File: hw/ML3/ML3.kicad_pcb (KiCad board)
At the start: 2 copper layers, 130 x 56 mm, 73 parts, among them J1 DE9_Receptacle, J2 PJ-102AH, J3 Conn_01x20, J4 Conn_01x02, Q1 DMG2305UX-13, SW0 TS04-66-55-BK-160-SMT, T1 Transformer_1P_1S, T2 Transformer_1P_1S, U1 LMV324 (Actually LTV9161), U2 LTV-356T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

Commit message: Added documentation about isolation - no board changes
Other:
- board text added: "NOTE: This break creates electrical isolation between the radio and the rest of the board."
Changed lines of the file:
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@@
+	)
+	(gr_line
+		(start 218.5 33.25)
+		(end 219.5 43.5)
+		(stroke
+			(width 0.15)
+			(type default)
+		)
+		(layer "Dwgs.User")
 	)
 	(gr_line
@@
 	)
 	(gr_line
-		(start 232.45 38.25)
-		(end 243.5 57.25)
+		(start 260 41)
+		(end 250 66.75)
 		(stroke
 			(width 0.3)
@@
 	)
 	(gr_text "J1: Radio connection (DB9)"
-		(at 223 37.25 0)
+		(at 257 38.25 0)
 		(layer "Dwgs.User")
 		(effects
@@
 		)
 	)
+	(gr_text "NOTE: This break creates electrical \nisolation between the radio and the \nrest of the board."
+		(at 205.5 33 0)
+		(layer "Dwgs.User")
+		(effects
+			(font
+				(size 1.5 1.5)
+				(thickness 0.2)
+				(bold yes)
+			)
+			(justify left bottom)
+		)
+	)
 	(gr_text "Micro USB Connection\n(NOTE: Bonded to Pico Pi daughter\ncard, so elevated from main PCB\nby 1.0mm)"
 		(at 137 37 0)
@@
 		)
 	)
-	(gr_text_box "External Connectors:\n1. J1 is a DB9 audio/signal connector connector.\n2. J2 is a 5.5mm DC power connector for +12V.  Center positive.\n3. The micro USB connector on the Pi Pico daughter card must be accessible through case.\n\nIndicator Notes:\n4. There are three SMD LEDs (D1, D3, D4).  External visibilty is required.\n\nThermal Notes:\n5. Air flow in the area of the LDO regulator (U3) is necessary.\n\nOther notes:\n6. Connector J3 is for testing.  Pin header will be populated.\n7. Trim protentiometers RV1, RV2 do not need to be accessible through case.\n8. Switch SW0 is used for programming and does not need to accessible through case.\n9. Connector J4 is an additional power output that is only used for diagnostics - not accessible through case.\n10. There are through-hole components on the PCB that result in leads/solder protroding from the bottom of the PCB. Leave about 5mm of clearance under the board.\n11. User adjustments on the top side of the PCB will be necessary during initial instalation (switches, trim pots).  The top of the case must be fairly easy to remove. "
+	(gr_text_box "External Connectors:\n1. J1 is a DB9 audio/signal connector connector.\n2. J2 is a 5.5mm DC power connector for +12V.  Center positive.\n3. The micro USB connector on the Pi Pico daughter card must be accessible through case.\n\nIndicator Notes:\n4. There are three SMD LEDs (D1, D3, D4).  External visibilty is required.\n\nThermal Notes:\n5. Air flow in the area of the LDO regulator (U3) is necessary.\n\nOther notes:\n6. Connector J3 is for testing.  Pin header will be populated.\n7. Trim protentiometers RV1, RV2 do not need to be accessible through case.\n8. Switch SW0 is used for programming and does not need to accessible through case.\n9. Connector J4 is an additional power output that is only used for diagnostics - not accessible through case.\n10. There are through-hole components on the PCB that result in leads/solder protroding from the bottom of the PCB. Leave about 5mm of clearance under the board.\n11. User adjustments on the top side of the PCB will be necessary during initial instalation (switches, trim pots).  The top of the case must be fairly easy to remove. \n12. The requirement for electrical isolation between the left and right sides of the board means that mounting (at least on the right) must be non-conductive."
 		(start 78 42)
-		(end 112 105)
-		(layer "Dwgs.User")
-		(effects
+		(end 112 113.25)
+		(layer "Dwgs.User")
+		(effects

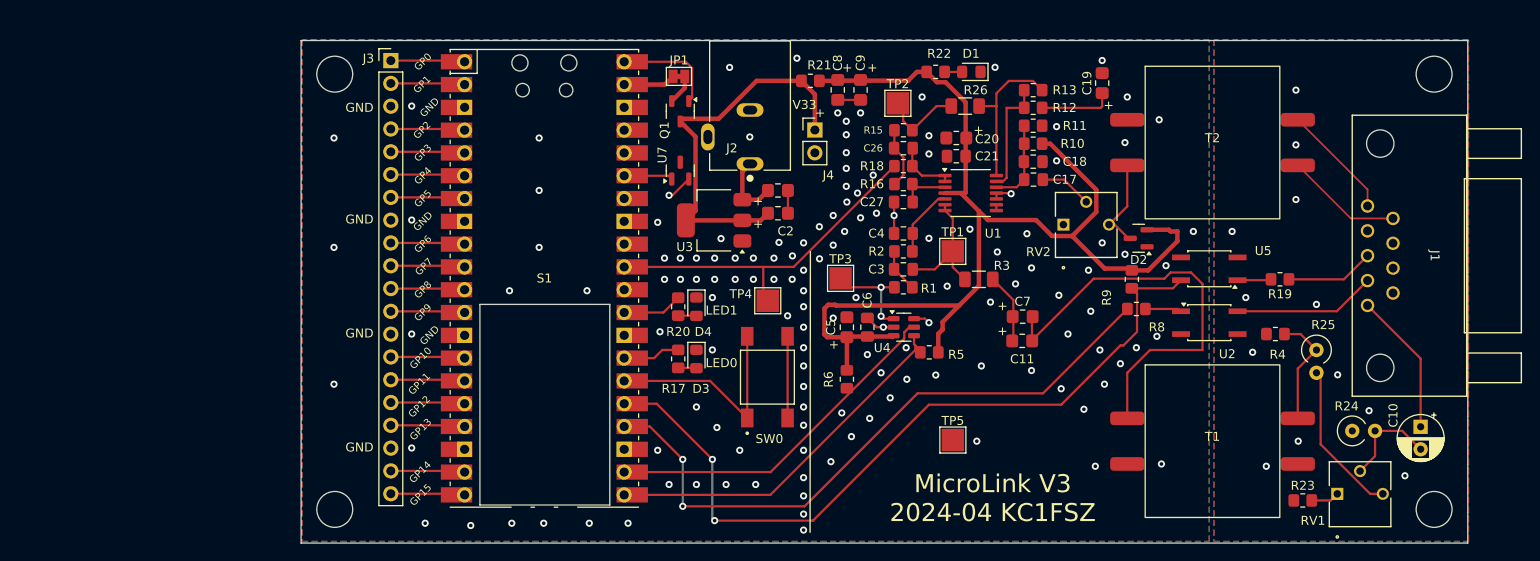
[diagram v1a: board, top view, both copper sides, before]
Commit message: V3 R1 incorporating connector moves from Steve
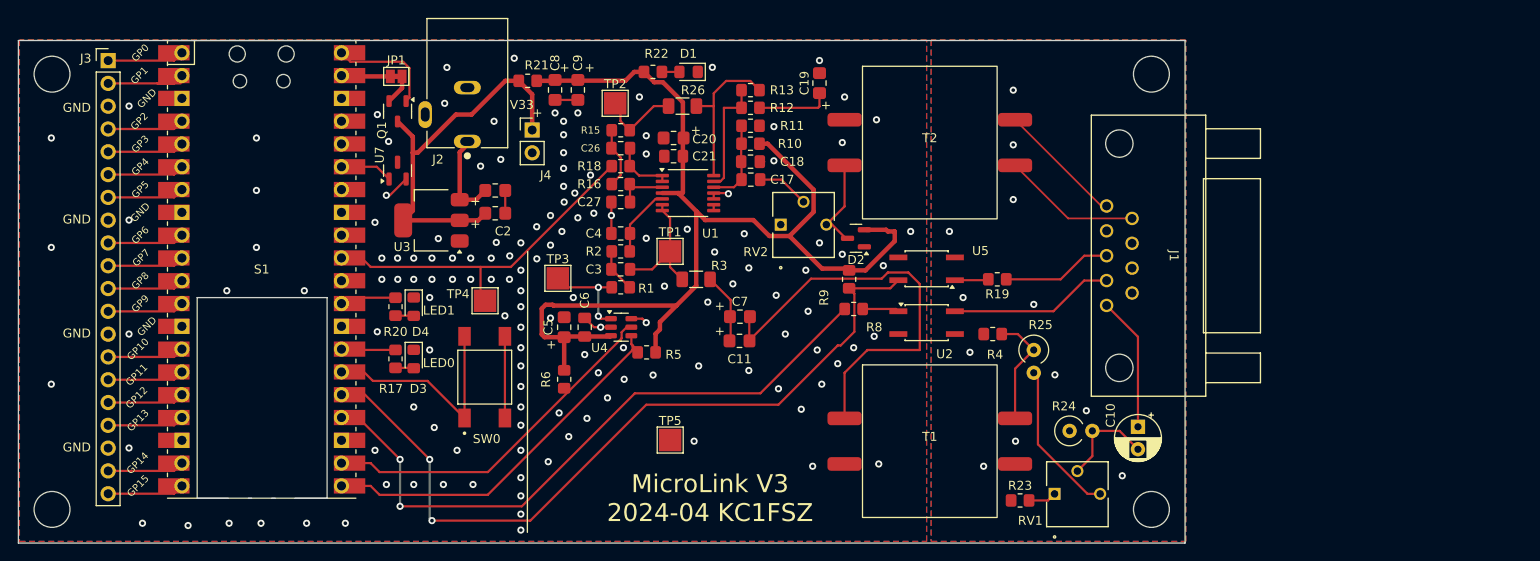
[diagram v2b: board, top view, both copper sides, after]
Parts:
- moved J2 31.6 mm to (136.5, 48.8)
- moved S1 31.5 mm to (113.6, 69.5)
- moved C1 31.5 mm to (139.6, 60.7)
- moved C10 31.5 mm to (211.2, 87.0)
- moved C11 31.5 mm to (166.9, 77.5)
- moved C17 31.5 mm to (168.1, 59.5)
- moved C18 31.5 mm to (168.1, 57.5)
- moved C19 31.5 mm to (175.8, 48.7)
- moved C2 31.5 mm to (139.6, 63.2)
- moved C20 31.5 mm to (159.5, 54.9)
- moved C21 31.5 mm to (159.5, 56.9)
- moved C26 31.5 mm to (153.6, 56.0)
- moved C27 31.5 mm to (153.6, 62.0)
- moved C3 31.5 mm to (153.6, 69.5)
- moved C4 31.5 mm to (153.6, 65.5)
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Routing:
- net Net-(J3-Pin_2): track 8.27 -> 13.0 mm
- net RIG_AF_OUT-: track 13.1 -> 15.5 mm
- net RIG_PTT: track 15.9 -> 18.3 mm
- net RIG_COS: track 9.84 -> 12.3 mm
- net +5VA: track 8.18 -> 9.77 mm
- net RIG_AF_OUT+: track 12.8 -> 14.2 mm
- net RIG_AF_IN: track 16.0 -> 15.0 mm
- net +3.3V: track 43.8 -> 42.9 mm
- net GNDA: vias 139 -> 144
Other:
- outline, holes or cut-outs redrawn
